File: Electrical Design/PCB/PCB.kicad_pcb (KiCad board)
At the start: 2 copper layers, 57 parts, among them J1 Conn_02x03_Odd_Even, J2 10118193-0001LF, M1 Camera_Servo, M2 Release_Servo, Q1 LED_MOS, Q2 CAMERA_MOS, Q3 RELEASE_MOS, Q4 BUZZER_MOS, U1 ADP3338AKCZ-5-R7, U2 BNO080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

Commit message: Update
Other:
- net class Default: clearance 0.2 -> 0.1524; trace_width 0.25 -> 0.1524; via_dia 0.8 -> 0.6858; via_drill 0.4 -> 0.3302
- rule pad_to_mask_clearance: 0.051 -> 0.0508
- rule trace_clearance: 0.2 -> 0.1524
- rule trace_min: 0.2 -> 0.1524
- rule via_min_drill: 0.3 -> 0.254
- rule via_min_size: 0.4 -> 0.508
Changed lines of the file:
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@@
   (title_block
     (title "Skfire PCB")
+    (date 2019-02-07)
     (rev v01)
     (company "UAH Space Hardware Club")
@@
   )
   (setup
-    (last_trace_width 0.25)
-    (trace_clearance 0.2)
+    (last_trace_width 0.1524)
+    (trace_clearance 0.1524)
     (zone_clearance 0.508)
     (zone_45_only no)
-    (trace_min 0.2)
+    (trace_min 0.1524)
     (segment_width 0.2)
     (edge_width 0.15)
-    (via_size 0.8)
-    (via_drill 0.4)
-    (via_min_size 0.4)
-    (via_min_drill 0.3)
-    (uvia_size 0.3)
-    (uvia_drill 0.1)
+    (via_size 0.6858)
+    (via_drill 0.3302)
+    (via_min_size 0.508)
+    (via_min_drill 0.254)
+    (uvia_size 0.6858)
+    (uvia_drill 0.3302)
     (uvias_allowed no)
     (uvia_min_size 0.2)
@@
     (pad_size 1.524 1.524)
     (pad_drill 0.762)
-    (pad_to_mask_clearance 0.051)
-    (solder_mask_min_width 0.25)
+    (pad_to_mask_clearance 0.0508)
     (aux_axis_origin 0 0)
     (visible_elements FFFFFF7F)
@@
   (net 95 "Net-(U9-Pad44)")
   (net_class Default "This is the default net class."
-    (clearance 0.2)
-    (trace_width 0.25)
-    (via_dia 0.8)
-    (via_drill 0.4)
-    (uvia_dia 0.3)
-    (uvia_drill 0.1)
+    (clearance 0.1524)
+    (trace_width 0.1524)
+    (via_dia 0.6858)
+    (via_drill 0.3302)
+    (uvia_dia 0.6858)
+    (uvia_drill 0.3302)
     (add_net +3V3)
     (add_net +5V)

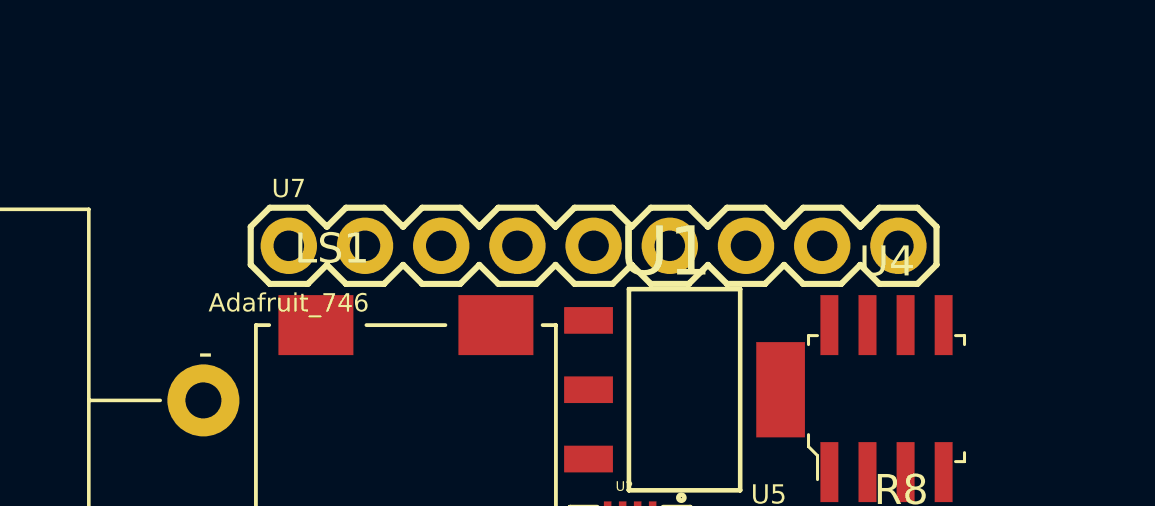
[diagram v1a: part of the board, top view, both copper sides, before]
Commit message: Generated initial PCB from schematic
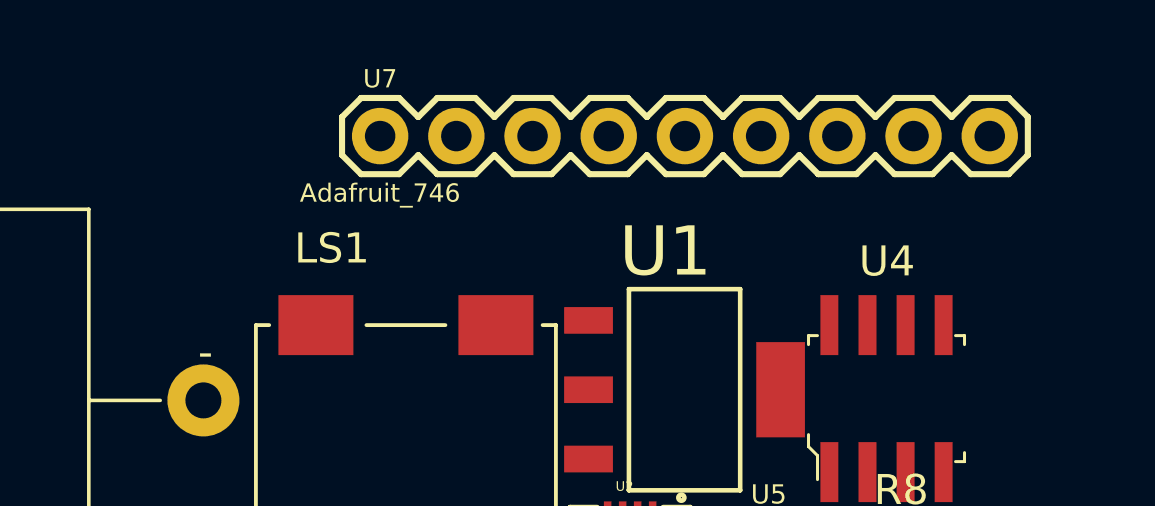
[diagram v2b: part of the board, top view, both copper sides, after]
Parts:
- moved U7 4.76 mm to (-244.1, 46.0)
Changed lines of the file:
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@@
-(kicad_pcb (version 20171130) (host pcbnew "(5.0.1-3-g963ef8bb5)")
+(kicad_pcb (version 20171130) (host pcbnew "(5.0.0)")
   (general
     (thickness 1.6)
@@
     (pad_to_mask_clearance 0.0508)
     (aux_axis_origin 0 0)
-    (visible_elements FFFFFF7F)
+    (visible_elements 7FFFFFFF)
     (pcbplotparams
       (layerselection 0x010fc_ffffffff)
@@
   )
   (module Connectors:1X09 (layer F.Cu)
-    (at -247.138399 49.631601)
+    (at -244.094 45.974)
     (descr "PLATED THROUGH HOLE -9 PIN")
     (tags "PLATED THROUGH HOLE -9 PIN")

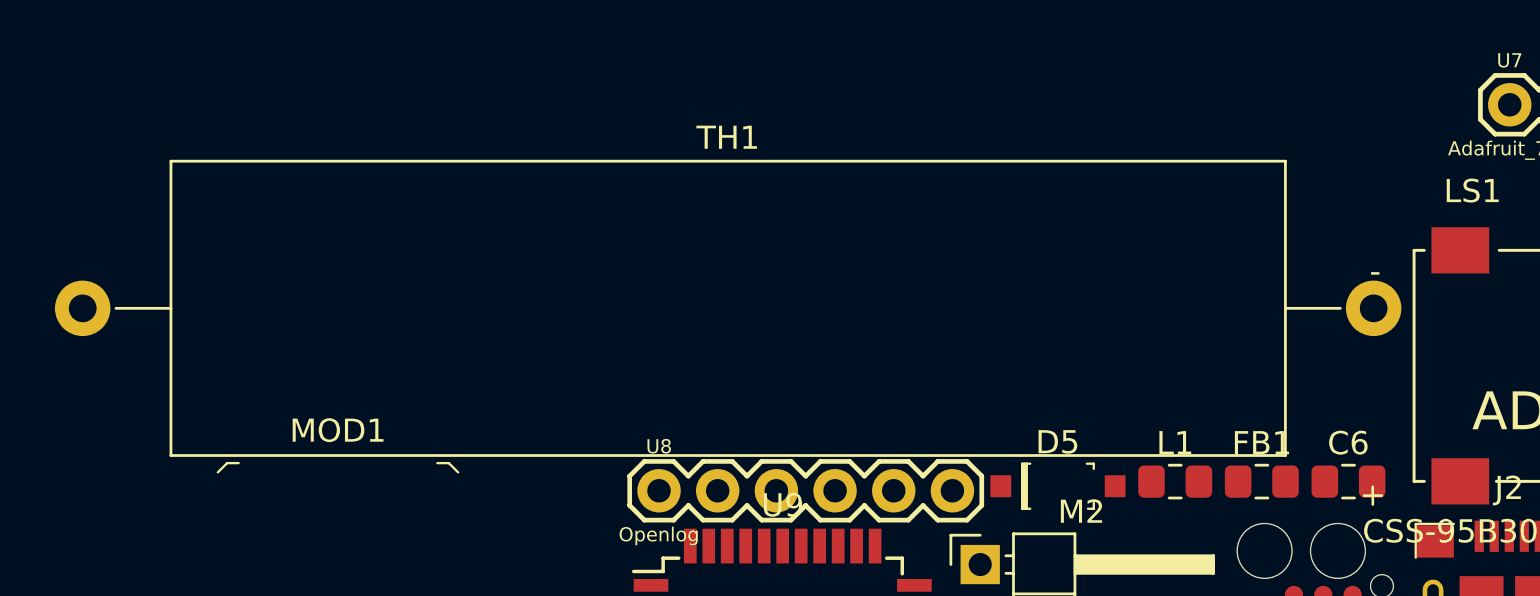
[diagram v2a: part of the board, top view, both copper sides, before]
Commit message: Update Thermistor Footprint
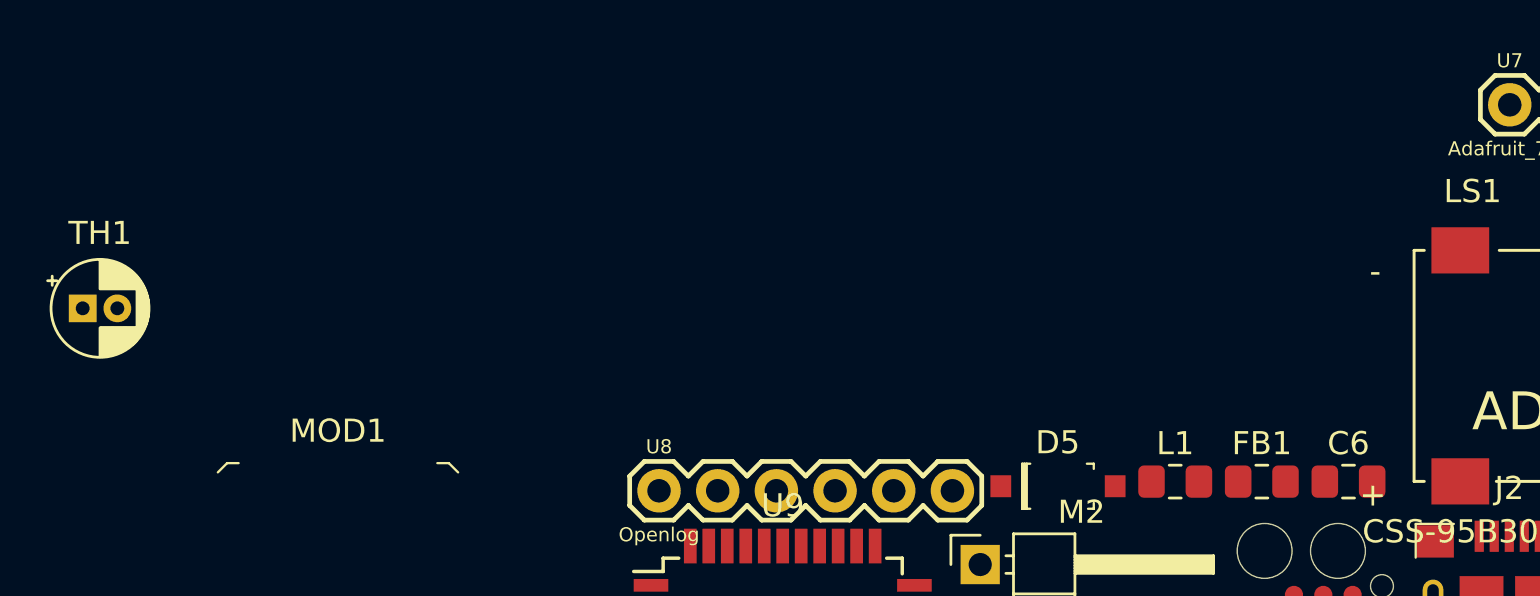
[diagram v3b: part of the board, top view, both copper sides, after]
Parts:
- TH1: footprint Resistor_THT:R_Axial_Power_L48.0mm_W12.5mm_P55.88mm -> Capacitor_THT:CP_Radial_D4.0mm_P1.50mm

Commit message: Spread Components
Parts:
- moved J1 513.6 mm to (261.0, 88.9)
- moved C13 501.4 mm to (232.4, 129.5)
- moved J2 496.2 mm to (252.1, 63.4)
- moved U5 470.9 mm to (240.0, 50.8)
- moved R2 466.8 mm to (228.8, 62.2)
- moved LS1 466.6 mm to (221.0, 104.1)
- moved C4 465.9 mm to (239.0, 72.4)
- moved R8 465.6 mm to (238.8, 67.3)
- moved R4 459.3 mm to (221.2, 61.0)
- moved R1 459.2 mm to (221.2, 68.6)
- moved U6 453.7 mm to (170.2, 139.7)
- moved U4 453.3 mm to (226.1, 49.5)
- moved R7 452.9 mm to (218.7, 73.7)
- moved C1 452.2 mm to (218.7, 81.3)
- moved R6 448.0 mm to (213.6, 50.8)
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
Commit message: Placement
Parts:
- moved Q1 103.8 mm to (86.1, 38.4)
- moved D1 83.3 mm to (104.5, 38.1)
- moved U3 64.3 mm to (106.7, 83.8)
- moved M2 29.0 mm to (102.9, 62.2)
- moved D3 26.4 mm to (104.5, 22.9)
- moved D2 26.2 mm to (104.5, 33.0)
- moved D4 25.8 mm to (104.5, 27.9)
- moved U9 21.6 mm to (109.2, 113.0)
- moved M1 21.1 mm to (102.9, 49.5)
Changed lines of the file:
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@@
   )
   (module LED_SMD:LED_0603_1608Metric_Pad1.05x0.95mm_HandSolder (layer F.Cu)
-    (at 164.690001 95.665001)
+    (at 104.535 38.1)
     (descr "LED SMD 0603 (1608 Metric), square (rectangular) end terminal, IPC_7351 nominal, (Body size source: http://www.tortai-tech.com/upload/download/2011102023233369053.pdf), generated with kicad-footprint-generator")
     (tags "LED handsolder")
@@
   )
   (module LED_SMD:LED_0603_1608Metric_Pad1.05x0.95mm_HandSolder (layer F.Cu)
-    (at 121.045 53.34)
+    (at 104.535 33.02)
     (descr "LED SMD 0603 (1608 Metric), square (rectangular) end terminal, IPC_7351 nominal, (Body size source: http://www.tortai-tech.com/upload/download/2011102023233369053.pdf), generated with kicad-footprint-generator")
     (tags "LED handsolder")
@@
   )
   (module LED_SMD:LED_0603_1608Metric_Pad1.05x0.95mm_HandSolder (layer F.Cu)
-    (at 122.795 41.91)
+    (at 104.535 22.86)
     (descr "LED SMD 0603 (1608 Metric), square (rectangular) end terminal, IPC_7351 nominal, (Body size source: http://www.tortai-tech.com/upload/download/2011102023233369053.pdf), generated with kicad-footprint-generator")
     (tags "LED handsolder")
@@
   )
   (module LED_SMD:LED_0603_1608Metric_Pad1.05x0.95mm_HandSolder (layer F.Cu)
-    (at 121.92 46.99)
+    (at 104.535 27.94)
     (descr "LED SMD 0603 (1608 Metric), square (rectangular) end terminal, IPC_7351 nominal, (Body size source: http://www.tortai-tech.com/upload/download/2011102023233369053.pdf), generated with kicad-footprint-generator")
     (tags "LED handsolder")
@@
   )
   (module Connector_PinHeader_2.54mm:PinHeader_1x03_P2.54mm_Horizontal (layer F.Cu)
-    (at 91.44 67.31)
+    (at 102.87 49.53)
     (descr "Through hole angled pin header, 1x03, 2.54mm pitch, 6mm pin length, single row")
     (tags "Through hole angled pin header THT 1x03 2.54mm single row")
@@
   )
   (module Connector_PinHeader_2.54mm:PinHeader_1x03_P2.54mm_Horizontal (layer F.Cu)
-    (at 130.81 69.85)
+    (at 102.87 62.23)
     (descr "Through hole angled pin header, 1x03, 2.54mm pitch, 6mm pin length, single row")
     (tags "Through hole angled pin header THT 1x03 2.54mm single row")
@@
   )
   (module digikey-footprints:SOT-23-3 (layer F.Cu)
-    (at 181.570001 79.145001)
+    (at 86.14 38.42)
     (fp_text reference Q1 (at 0.025 -3.375) (layer F.SilkS)
       (effects (font (size 1 1) (thickness 0.15)))
@@
   )
   (module ADP3338AKCZ-3.3RL7:SOT230P700X180-4N (layer F.Cu)
-    (at 162.56 115.57)
+    (at 106.68 83.82)
     (attr smd)
     (fp_text reference U3 (at -0.63534 -4.59985) (layer F.SilkS)
@@
   )
   (module Package_QFP:TQFP-44_10x10mm_P0.8mm (layer F.Cu)
-    (at 124.46 128.27)
+    (at 109.22 113.03)
     (descr "44-Lead Plastic Thin Quad Flatpack (PT) - 10x10x1.0 mm Body [TQFP] (see Microchip Packaging Specification 00000049BS.pdf)")
     (tags "QFP 0.8")

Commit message: Batteries and Camera
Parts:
- added U10: Adafruit_Cam, Connectors:MOLEX-1X3, F.Cu at (13.9, -83.2)
- added U11: BH123A, BH123A:BH123A, F.Cu at (-8.95, -77.4)
- added U12: BH123A, BH123A:BH123A, F.Cu at (-8.95, -59.5)
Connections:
- U9 pad 43: Net-(U9-Pad43) -> /CAMERA_DATA
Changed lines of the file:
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@@
-(kicad_pcb (version 20171130) (host pcbnew 5.0.2-bee76a0~70~ubuntu18.04.1)
+(kicad_pcb (version 20171130) (host pcbnew "(5.0.1-3-g963ef8bb5)")
   (general
     (thickness 1.6)
@@
     (tracks 0)
     (zones 0)
-    (modules 57)
-    (nets 96)
+    (modules 60)
+    (nets 97)
   )
   (page A4)
@@
   (net 92 "Net-(U9-Pad36)")
   (net 93 "Net-(U9-Pad37)")
-  (net 94 "Net-(U9-Pad43)")
-  (net 95 "Net-(U9-Pad44)")
+  (net 94 "Net-(U9-Pad44)")
+  (net 95 /CAMERA_DATA)
+  (net 96 "Net-(U11-Pad-)")
   (net_class Default "This is the default net class."
     (clearance 0.1524)
@@
     (add_net /BNO_WAKE)
     (add_net /BUZZER_MOS)
+    (add_net /CAMERA_DATA)
     (add_net /CAMERA_MOS)
     (add_net /Camera_Servo)
@@
     (add_net "Net-(Q4-Pad1)")
     (add_net "Net-(R6-Pad2)")
+    (add_net "Net-(U11-Pad-)")
     (add_net "Net-(U2-Pad15)")
     (add_net "Net-(U2-Pad16)")
@@
     (add_net "Net-(U9-Pad37)")
     (add_net "Net-(U9-Pad4)")
-    (add_net "Net-(U9-Pad43)")
     (add_net "Net-(U9-Pad44)")
     (add_net "Net-(U9-Pad5)")
@@
     (add_net "Net-(U9-Pad7)")
   )
+  (module BH123A:BH123A (layer F.Cu)
+    (at -8.953499 -59.506499)
+    (fp_text reference U12 (at 0 0) (layer F.SilkS)
+      (effects (font (size 1 0.9) (thickness 0.05)))
+    )
+    (fp_text value BH123A (at -18.415 -10.795) (layer F.SilkS)
+      (effects (font (size 1 1) (thickness 0.05)))
+    )
+    (fp_text user BH123A (at -3.81 -1.27) (layer Cmts.User)
+      (effects (font (size 1 1) (thickness 0.05)))
+    )
+    (fp_line (start 21.463 8.89) (end 21.463 -8.89) (layer F.SilkS) (width 0.127))
+    (fp_line (start -21.463 8.89) (end 21.463 8.89) (layer F.SilkS) (width 0.127))
+    (fp_line (start -21.463 -8.89) (end -21.463 8.89) (layer F.SilkS) (width 0.127))
+    (fp_line (start 21.463 -8.89) (end -21.463 -8.89) (layer F.SilkS) (width 0.127))
+    (pad Hole np_thru_hole circle (at 19.558 6.35) (size 1.27 1.27) (drill 1.27) (layers *.Cu *.Mask F.SilkS))
+    (pad + thru_hole rect (at 18.9738 0) (size 2.54 2.54) (drill 1.524) (layers *.Cu *.Mask)
+      (net 96 "Net-(U11-Pad-)"))
+    (pad - thru_hole rect (at -18.9738 0) (size 2.54 2.54) (drill 1.524) (layers *.Cu *.Mask)
+      (net 1 GND))
+  )
+  (module BH123A:BH123A (layer F.Cu)
+    (at -8.953499 -77.406499)
+    (fp_text reference U11 (at 0 0) (layer F.SilkS)
+      (effects (font (size 1 0.9) (thickness 0.05)))
+    )
+    (fp_text value BH123A (at -18.415 -10.795) (layer F.SilkS)
+      (effects (font (size 1 1) (thickness 0.05)))
+    )
+    (fp_line (start 21.463 -8.89) (end -21.463 -8.89) (layer F.SilkS) (width 0.127))
+    (fp_line (start -21.463 -8.89) (end -21.463 8.89) (layer F.SilkS) (width 0.127))
+    (fp_line (start -21.463 8.89) (end 21.463 8.89) (layer F.SilkS) (width 0.127))
+    (fp_line (start 21.463 8.89) (end 21.463 -8.89) (layer F.SilkS) (width 0.127))
+    (fp_text user BH123A (at -3.81 -1.27) (layer Cmts.User)
+      (effects (font (size 1 1) (thickness 0.05)))
+    )
+    (pad - thru_hole rect (at -18.9738 0) (size 2.54 2.54) (drill 1.524) (layers *.Cu *.Mask)
+      (net 96 "Net-(U11-Pad-)"))
+    (pad + thru_hole rect (at 18.9738 0) (size 2.54 2.54) (drill 1.524) (layers *.Cu *.Mask)
+      (net 2 +6V))
+    (pad Hole np_thru_hole circle (at 19.558 6.35) (size 1.27 1.27) (drill 1.27) (layers *.Cu *.Mask F.SilkS))
+  )
+  (module Connectors:MOLEX-1X3 (layer F.Cu)
+    (at 13.903501 -83.248499)
+    (descr "PTH - 3 PIN VERTICAL MOLEX POLARIZED HEADER")
+    (tags "PTH - 3 PIN VERTICAL MOLEX POLARIZED HEADER")
+    (attr virtual)
+    (fp_text reference U10 (at 0 -3.556) (layer F.SilkS)
+      (effects (font (size 0.6096 0.6096) (thickness 0.127)))
+    )
+    (fp_text value Adafruit_Cam (at 0 3.175) (layer F.SilkS)
+      (effects (font (size 0.6096 0.6096) (thickness 0.127)))
+    )
+    (fp_line (start -1.27 -3.048) (end -1.27 2.54) (layer F.SilkS) (width 0.127))
+    (fp_line (start 6.35 -3.048) (end 6.35 2.54) (layer F.SilkS) (width 0.127))
+    (fp_line (start 6.35 -3.048) (end -1.27 -3.048) (layer F.SilkS) (width 0.127))
+    (fp_line (start 6.35 2.54) (end 5.08 2.54) (layer F.SilkS) (width 0.127))
+    (fp_line (start 5.08 2.54) (end 0 2.54) (layer F.SilkS) (width 0.127))
+    (fp_line (start 0 2.54) (end -1.27 2.54) (layer F.SilkS) (width 0.127))
+    (fp_line (start 0 2.54) (end 0 1.27) (layer F.SilkS) (width 0.127))
+    (fp_line (start 0 1.27) (end 5.08 1.27) (layer F.SilkS) (width 0.127))
+    (fp_line (start 5.08 1.27) (end 5.08 2.54) (layer F.SilkS) (width 0.127))
+    (pad 1 thru_hole rect (at 0 0) (size 1.8796 1.8796) (drill 1.016) (layers *.Cu *.Mask)
+      (net 5 +5V) (solder_mask_margin 0.1016))
+    (pad 2 thru_hole circle (at 2.54 0) (size 1.8796 1.8796) (drill 1.016) (layers *.Cu *.Mask)
+      (net 1 GND) (solder_mask_margin 0.1016))
+    (pad 3 thru_hole circle (at 5.08 0) (size 1.8796 1.8796) (drill 1.016) (layers *.Cu *.Mask)
+      (net 95 /CAMERA_DATA) (solder_mask_margin 0.1016))
+  )
   (module Capacitor_SMD:C_0805_2012Metric_Pad1.15x1.40mm_HandSolder (layer F.Cu)
     (at 218.685 81.28)
@@
       (net 51 /CAMERA_MOS))
     (pad 43 smd rect (at -3.2 -5.7 90) (size 1.5 0.55) (layers F.Cu F.Paste F.Mask)
-      (net 94 "Net-(U9-Pad43)"))
+      (net 95 /CAMERA_DATA))
     (pad 44 smd rect (at -4 -5.7 90) (size 1.5 0.55) (layers F.Cu F.Paste F.Mask)
-      (net 95 "Net-(U9-Pad44)"))
+      (net 94 "Net-(U9-Pad44)"))
     (model ${KISYS3DMOD}/Package_QFP.3dshapes/TQFP-44_10x10mm_P0.8mm.wrl
       (at (xyz 0 0 0))

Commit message: PCB Layout
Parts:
- moved U5 245.0 mm to (19.1, 156.9)
- moved C4 228.1 mm to (20.3, 137.2)
- moved U10 200.2 mm to (20.3, 116.8)
- moved R1 198.8 mm to (23.1, 85.1)
- moved C12 179.7 mm to (24.4, 154.9)
- moved M2 157.0 mm to (255.8, 26.7)
- moved C7 156.4 mm to (20.6, 132.1)
- moved M1 154.1 mm to (256.8, 43.2)
- moved R7 147.4 mm to (82.8, 16.5)
- moved LS1 147.0 mm to (92.2, 175.2)
- moved R14 138.3 mm to (108.2, 168.9)
- moved U12 126.0 mm to (47.0, 53.3)
- moved C9 125.7 mm to (79.0, 81.3)
- moved C10 122.8 mm to (78.7, 77.5)
- moved U11 122.7 mm to (47.0, 31.8)
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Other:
- board outline added: 50 x 152 mm

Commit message: Update
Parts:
- U2: moved to B.Cu
- moved C5 159.8 mm to (170.2, 168.4), turned to 90 degrees
- moved C2 148.5 mm to (170.2, 162.3), turned to 90 degrees
- moved U2 137.6 mm to (156.9, 158.9), turned to 90 degrees
- moved C3 137.0 mm to (170.2, 156.2), turned to 90 degrees
- moved U5 131.0 mm to (150.1, 159.8)
- moved C12 120.7 mm to (145.0, 158.8), turned to 270 degrees
- moved C10 106.4 mm to (137.2, 166.4)
- moved MOD1 104.2 mm to (147.3, 159.3), turned to 90 degrees
- moved C9 101.2 mm to (137.2, 164.1), turned to 180 degrees
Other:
- board size 50 x 152 mm -> 50 x 150 mm
